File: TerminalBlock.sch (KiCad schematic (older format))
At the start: 0 parts

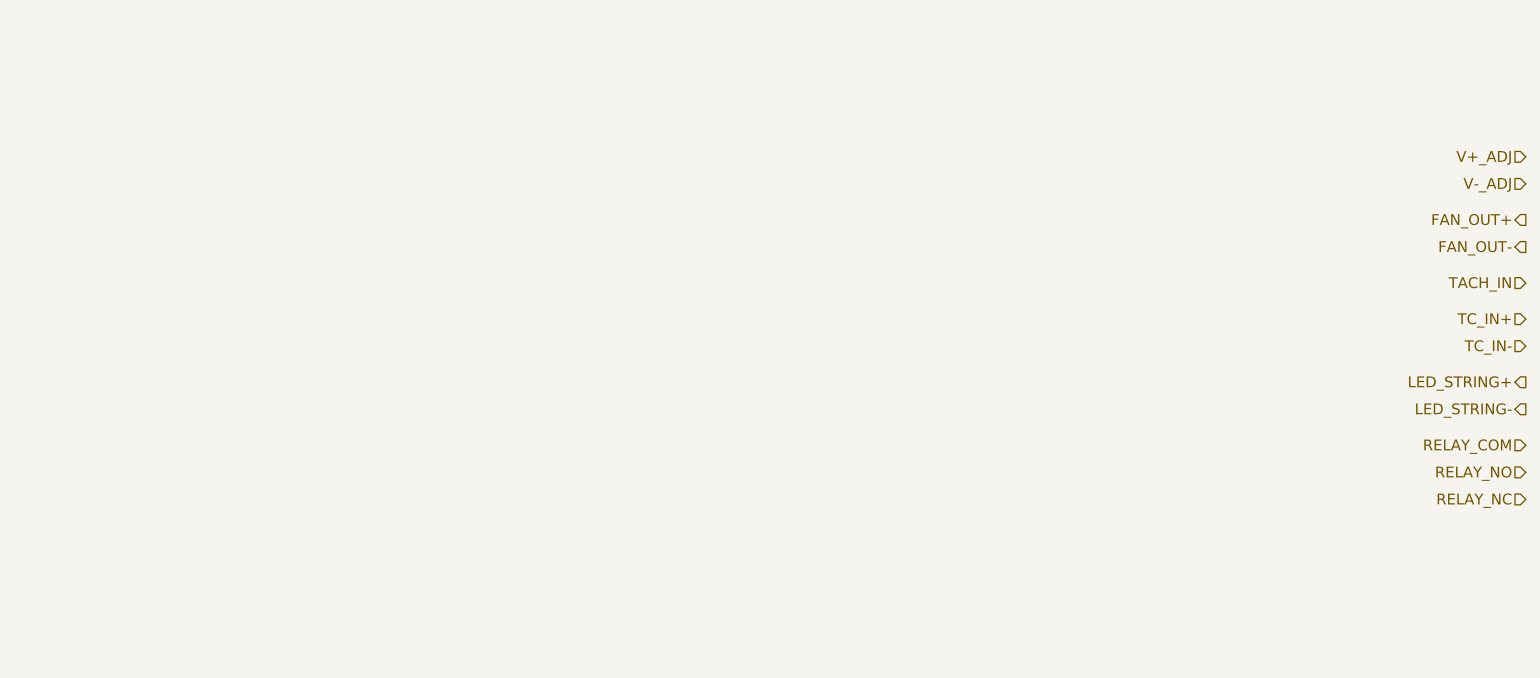
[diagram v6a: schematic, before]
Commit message: Plug Placement
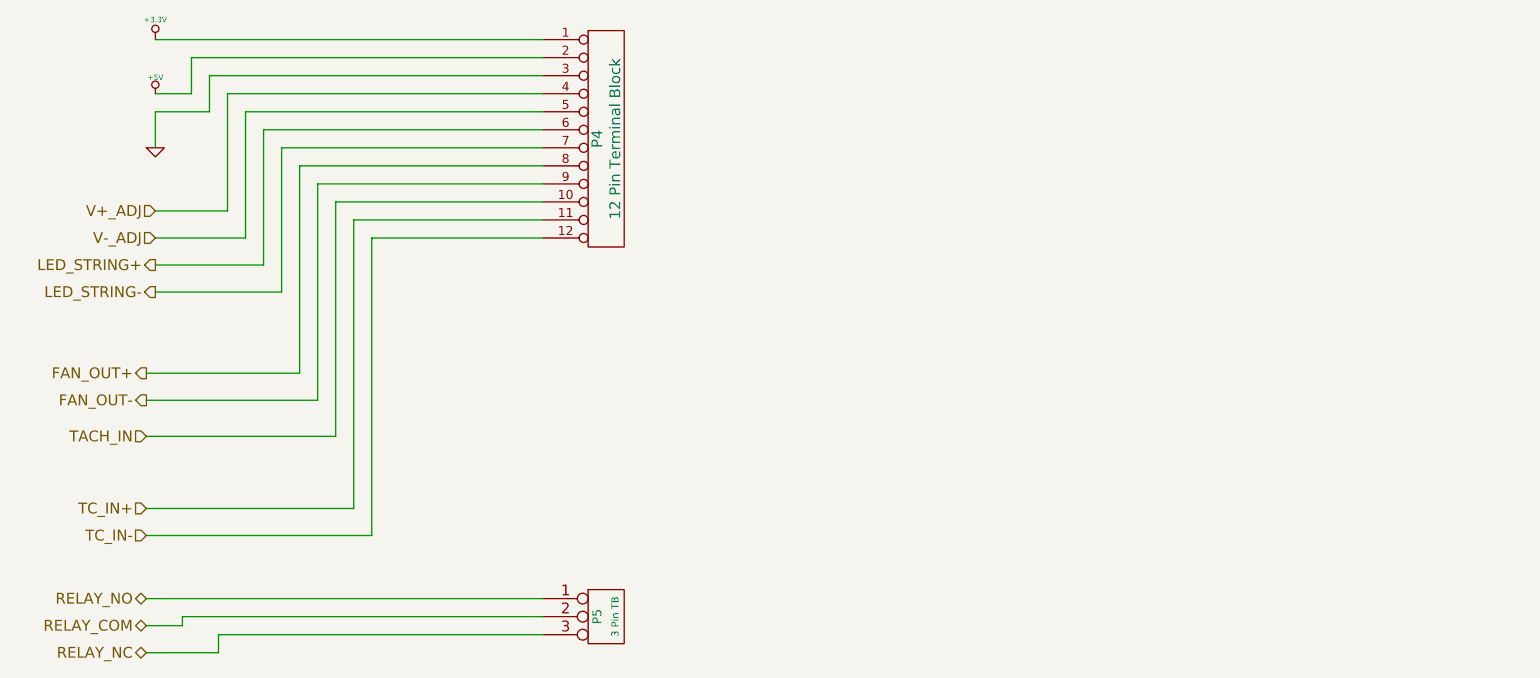
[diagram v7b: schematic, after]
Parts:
- added P4: 12 Pin Terminal Block, symbol CONN_12
- added P5: 3 Pin TB, symbol CONN_3
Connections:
- net FAN_OUT+: now also P4.8 (P8)
- net FAN_OUT-: now also P4.9 (P9)
- net LED_STRING+: now also P4.6 (P6)
- net LED_STRING-: now also P4.7 (P7)
- net RELAY_COM: now also P5.2 (PM)
- net RELAY_NC: now also P5.3 (P3)
- net RELAY_NO: now also P5.1 (P1)
- net TACH_IN: now also P4.10 (P10)
- net TC_IN+: now also P4.11 (P11)
- net TC_IN-: now also P4.12 (P12)
- net V+_ADJ: now also P4.4 (P4)
- net V-_ADJ: now also P4.5 (P5)
- new net +3.3V: P4.1 (P1)
- new net +5V: P4.2 (P2)
- new net GND: P4.3 (P3)
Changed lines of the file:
@@
 Sheet 9 9
 Title ""
-Date "15 oct 2013"
+Date "17 oct 2013"
 Rev ""
 Comp ""
@@
 Comment4 ""
 $EndDescr
-Text HLabel 10200 1400 0    60   Input ~ 0
+Text HLabel 2600 1700 0    60   Input ~ 0
 V+_ADJ
-Text HLabel 10200 1550 0    60   Input ~ 0
+Text HLabel 2600 1850 0    60   Input ~ 0
 V-_ADJ
-Text HLabel 10200 1750 0    60   Output ~ 0
+Text HLabel 2550 2600 0    60   Output ~ 0
 FAN_OUT+
-Text HLabel 10200 1900 0    60   Output ~ 0
+Text HLabel 2550 2750 0    60   Output ~ 0
 FAN_OUT-
-Text HLabel 10200 2100 0    60   Input ~ 0
+Text HLabel 2550 2950 0    60   Input ~ 0
 TACH_IN
-Text HLabel 10200 2300 0    60   Input ~ 0
+Text HLabel 2550 3350 0    60   Input ~ 0
 TC_IN+
-Text HLabel 10200 2450 0    60   Input ~ 0
+Text HLabel 2550 3500 0    60   Input ~ 0
 TC_IN-
-Text HLabel 10200 2650 0    60   Output ~ 0
+Text HLabel 2600 2000 0    60   Output ~ 0
 LED_STRING+
-Text HLabel 10200 2800 0    60   Output ~ 0
+Text HLabel 2600 2150 0    60   Output ~ 0
 LED_STRING-
-Text HLabel 10200 3000 0    60   Input ~ 0
+Text HLabel 2550 4000 0    60   BiDi ~ 0
 RELAY_COM
-Text HLabel 10200 3150 0    60   Input ~ 0
+Text HLabel 2550 3850 0    60   BiDi ~ 0
 RELAY_NO
-Text HLabel 10200 3300 0    60   Input ~ 0
+Text HLabel 2550 4150 0    60   BiDi ~ 0
 RELAY_NC
+$Comp
+L CONN_12 P4
+U 1 1 525E2337
+P 5100 1300
+F 0 "P4" V 5050 1300 60  0000 C CNN
+F 1 "12 Pin Terminal Block" V 5150 1300 60  0000 C CNN
+F 2 "" H 5100 1300 60  0000 C CNN
+F 3 "" H 5100 1300 60  0000 C CNN
+F 4 "On Shore" H 5100 1300 60  0001 C CNN "MFG Name"
+F 5 "OSTTE120104" H 5100 1300 60  0001 C CNN "MFG Part Number"
+	1    5100 1300
+	1    0    0    -1
+$EndComp
+$Comp
+L +3.3V #PWR057
+U 1 1 525E2346
+P 2600 750
+F 0 "#PWR057" H 2600 710 30  0001 C CNN
+F 1 "+3.3V" H 2600 860 30  0000 C CNN
+F 2 "" H 2600 750 60  0000 C CNN
+F 3 "" H 2600 750 60  0000 C CNN
+	1    2600 750
+	1    0    0    -1
+$EndComp
+$Comp
+L +5V #PWR058
+U 1 1 525E2355
+P 2600 1050
+F 0 "#PWR058" H 2600 1140 20  0001 C CNN
+F 1 "+5V" H 2600 1140 30  0000 C CNN
+F 2 "" H 2600 1050 60  0000 C CNN
+F 3 "" H 2600 1050 60  0000 C CNN
+	1    2600 1050
+	1    0    0    -1
+$EndComp
+$Comp
+L GND #PWR059
+U 1 1 525E2364
+P 2600 1350
+F 0 "#PWR059" H 2600 1350 30  0001 C CNN
+F 1 "GND" H 2600 1280 30  0001 C CNN
+F 2 "" H 2600 1350 60  0000 C CNN
+F 3 "" H 2600 1350 60  0000 C CNN
+	1    2600 1350
+	1    0    0    -1
+$EndComp
+Wire Wire Line
+	2600 750  4750 750
+Wire Wire Line
+	4750 850  2800 850
+Wire Wire Line
+	2800 850  2800 1050
+Wire Wire Line
+	2800 1050 2600 1050
+Wire Wire Line
+	2600 1350 2600 1150
+Wire Wire Line
+	2600 1150 2900 1150
+Wire Wire Line
+	2900 1150 2900 950
+Wire Wire Line
+	2900 950  4750 950
+Wire Wire Line
+	2600 1700 3000 1700
+Wire Wire Line
+	3000 1700 3000 1050
+Wire Wire Line
+	3000 1050 4750 1050
+Wire Wire Line
+	2600 1850 3100 1850
+Wire Wire Line
+	3100 1850 3100 1150
+Wire Wire Line
+	3100 1150 4750 1150
+Wire Wire Line
+	4750 1250 3200 1250
+Wire Wire Line
+	3200 1250 3200 2000
+Wire Wire Line
+	3200 2000 2600 2000
+Wire Wire Line
+	2600 2150 3300 2150
+Wire Wire Line
+	3300 2150 3300 1350
+Wire Wire Line
+	3300 1350 4750 1350
+Wire Wire Line
+	2550 2600 3400 2600
+Wire Wire Line
+	3400 2600 3400 1450
+Wire Wire Line
+	3400 1450 4750 1450
+Wire Wire Line
+	4750 1550 3500 1550
+Wire Wire Line
+	3500 1550 3500 2750
+Wire Wire Line
+	3500 2750 2550 2750
+Wire Wire Line
+	2550 2950 3600 2950
+Wire Wire Line
+	3600 2950 3600 1650
+Wire Wire Line
+	3600 1650 4750 1650
+Wire Wire Line
+	4750 1750 3700 1750
+Wire Wire Line
+	3700 1750 3700 3350
+Wire Wire Line
+	3700 3350 2550 3350
+Wire Wire Line
+	2550 3500 3800 3500
+Wire Wire Line
+	3800 3500 3800 1850
+Wire Wire Line
+	3800 1850 4750 1850
+$Comp
+L CONN_3 P5
+U 1 1 525E2773
+P 5100 3950
+F 0 "P5" V 5050 3950 50  0000 C CNN
+F 1 "3 Pin TB" V 5150 3950 40  0000 C CNN
+F 2 "" H 5100 3950 60  0000 C CNN
+F 3 "" H 5100 3950 60  0000 C CNN
+F 4 "Phoenix" H 5100 3950 60  0001 C CNN "MFG Name"
+F 5 "1935174" H 5100 3950 60  0001 C CNN "MFG Part Number"
+	1    5100 3950
+	1    0    0    -1
+$EndComp
+Wire Wire Line
+	2550 3850 4750 3850
+Wire Wire Line
+	4750 3950 2750 3950
+Wire Wire Line
+	2750 3950 2750 4000
+Wire Wire Line
+	2750 4000 2550 4000
+Wire Wire Line
+	2550 4150 2950 4150
+Wire Wire Line
+	2950 4150 2950 4050
+Wire Wire Line
+	2950 4050 4750 4050
 $EndSCHEMATC
